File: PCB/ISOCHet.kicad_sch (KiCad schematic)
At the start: 19 parts, among them J1 USB_C_Receptacle_USB2.0, J2 Conn_01x08_Pin, SW0 BOOT, SW1 TAB, SW2 ENTER, SW3 CAPS, SW4 CAPS_STEP1.5, SW5 CAPS_STEP1.25, U1 CH552G, U2 USBLC6-2P6

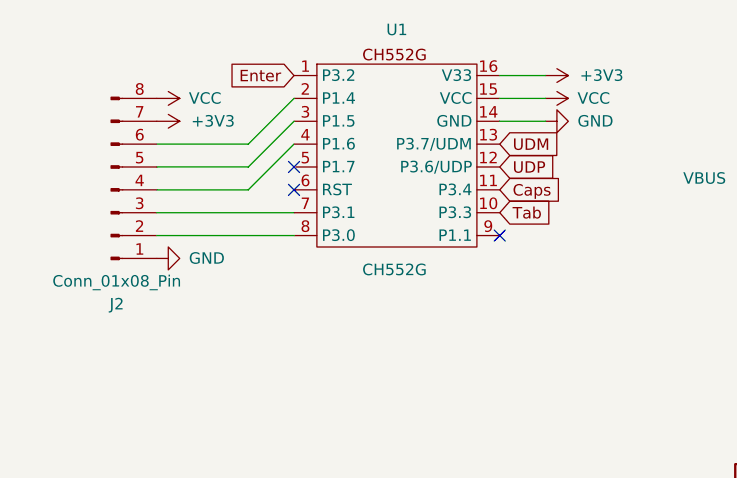
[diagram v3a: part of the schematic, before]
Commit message: Move components
 * Move decoupling capacitor C1 close to U1
 * Move U1 away from PCB edge
 * Align U1 with PCB centreline
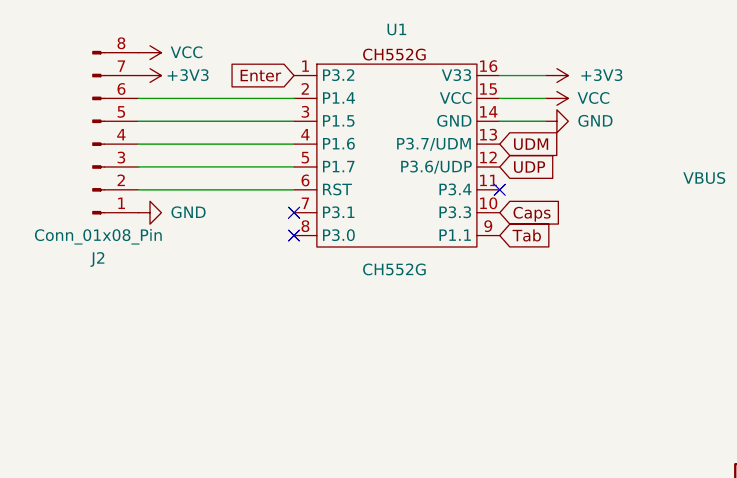
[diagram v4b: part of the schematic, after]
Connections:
- net Caps: now also U1.10 (P3.3); no longer U1.11 (P3.4)
- net Tab: now also U1.9 (P1.1); no longer U1.10 (P3.3)
- net at J2.2 (Pin_2): now also U1.6 (RST); no longer U1.8 (P3.0)
- net at J2.3 (Pin_3): now also U1.5 (P1.7); no longer U1.7 (P3.1)
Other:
- moved on the sheet: J2
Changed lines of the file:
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@@
   (junction (at 60.96 118.11) (diameter 0) (color 0 0 0 0)
   )
+  (no_connect (at 42.164 54.61))
   (no_connect (at 60.96 134.62))
-  (no_connect (at 42.164 46.99))
-  (no_connect (at 65.024 54.61))
+  (no_connect (at 65.024 49.53))
   (no_connect (at 60.96 132.08))
-  (no_connect (at 42.164 49.53))
+  (no_connect (at 42.164 52.07))
   (wire (pts (xy 120.65 48.26) (xy 115.57 48.26))
     (stroke (width 0) (type default))
@@
     (stroke (width 0) (type default))
   )
-  (wire (pts (xy 26.924 49.53) (xy 37.084 49.53))
-    (stroke (width 0) (type default))
-  )
   (wire (pts (xy 60.96 118.11) (xy 60.96 119.38))
     (stroke (width 0) (type default))
@@
     (stroke (width 0) (type default))
   )
-  (wire (pts (xy 26.924 46.99) (xy 37.084 46.99))
+  (wire (pts (xy 24.892 46.99) (xy 42.164 46.99))
     (stroke (width 0) (type default))
   )
@@
     (stroke (width 0) (type default))
   )
+  (wire (pts (xy 24.892 39.37) (xy 42.164 39.37))
+    (stroke (width 0) (type default))
+  )
   (wire (pts (xy 116.586 109.22) (xy 119.126 109.22))
     (stroke (width 0) (type default))
@@
     (stroke (width 0) (type default))
   )
-  (wire (pts (xy 26.924 52.07) (xy 42.164 52.07))
-    (stroke (width 0) (type default))
-  )
-  (wire (pts (xy 26.924 54.61) (xy 42.164 54.61))
-    (stroke (width 0) (type default))
-  )
   (wire (pts (xy 65.024 36.83) (xy 70.104 36.83))
     (stroke (width 0) (type default))
   )
-  (wire (pts (xy 37.084 46.99) (xy 42.164 41.91))
-    (stroke (width 0) (type default))
-  )
   (wire (pts (xy 115.57 53.34) (xy 115.57 48.26))
     (stroke (width 0) (type default))
@@
     (stroke (width 0) (type default))
   )
-  (wire (pts (xy 37.084 49.53) (xy 42.164 44.45))
-    (stroke (width 0) (type default))
-  )
   (wire (pts (xy 123.19 60.96) (xy 123.19 63.5))
     (stroke (width 0) (type default))
@@
     (stroke (width 0) (type default))
   )
+  (wire (pts (xy 24.892 41.91) (xy 42.164 41.91))
+    (stroke (width 0) (type default))
+  )
   (wire (pts (xy 71.374 111.76) (xy 60.96 111.76))
     (stroke (width 0) (type default))
@@
     (stroke (width 0) (type default))
   )
-  (wire (pts (xy 37.084 44.45) (xy 42.164 39.37))
-    (stroke (width 0) (type default))
-  )
-  (wire (pts (xy 26.924 44.45) (xy 37.084 44.45))
+  (wire (pts (xy 24.892 44.45) (xy 42.164 44.45))
     (stroke (width 0) (type default))
   )
   (wire (pts (xy 78.994 109.22) (xy 78.994 110.49))
+    (stroke (width 0) (type default))
+  )
+  (wire (pts (xy 24.892 49.53) (xy 42.164 49.53))
     (stroke (width 0) (type default))
   )
@@
     )
   )
-  (global_label "Tab" (shape input) (at 65.024 52.07 0) (fields_autoplaced)
+  (global_label "Tab" (shape input) (at 65.024 54.61 0) (fields_autoplaced)
     (effects (font (size 1.27 1.27)) (justify left))
-    (property "Intersheetrefs" "${INTERSHEET_REFS}" (at 71.2748 52.07 0)
+    (property "Intersheetrefs" "${INTERSHEET_REFS}" (at 71.2748 54.61 0)
       (effects (font (size 1.27 1.27)) (justify left) hide)
     )
@@
     )
   )
-  (global_label "Caps" (shape input) (at 65.024 49.53 0) (fields_autoplaced)
+  (global_label "Caps" (shape input) (at 65.024 52.07 0) (fields_autoplaced)
     (effects (font (size 1.27 1.27)) (justify left))
-    (property "Intersheetrefs" "${INTERSHEET_REFS}" (at 72.6053 49.53 0)
+    (property "Intersheetrefs" "${INTERSHEET_REFS}" (at 72.6053 52.07 0)
       (effects (font (size 1.27 1.27)) (justify left) hide)
     )
@@
     )
   )
-  (symbol (lib_id "power:+3V3") (at 26.924 41.91 270) (unit 1)
+  (symbol (lib_id "power:+3V3") (at 24.892 36.83 270) (unit 1)
     (in_bom yes) (on_board yes) (dnp no)
-    (property "Reference" "#PWR020" (at 23.114 41.91 0)
-      (effects (font (size 1.27 1.27)) hide)
-    )
-    (property "Value" "+3V3" (at 30.734 41.91 90)
-      (effects (font (size 1.27 1.27)) (justify left))
-    )
-    (property "Footprint" "" (at 26.924 41.91 0)
-      (effects (font (size 1.27 1.27)) hide)
-    )
-    (property "Datasheet" "" (at 26.924 41.91 0)
+    (property "Reference" "#PWR020" (at 21.082 36.83 0)
+      (effects (font (size 1.27 1.27)) hide)
+    )
+    (property "Value" "+3V3" (at 27.94 36.83 90)
+      (effects (font (size 1.27 1.27)) (justify left))
+    )
+    (property "Footprint" "" (at 24.892 36.83 0)
+      (effects (font (size 1.27 1.27)) hide)
+    )
+    (property "Datasheet" "" (at 24.892 36.83 0)
       (effects (font (size 1.27 1.27)) hide)
     )
@@
     )
   )
-  (symbol (lib_id "power:VCC") (at 26.924 39.37 270) (unit 1)
-    (in_bom yes) (on_board yes) (dnp no) (fields_autoplaced)
-    (property "Reference" "#PWR022" (at 23.114 39.37 0)
-      (effects (font (size 1.27 1.27)) hide)
-    )
-    (property "Value" "VCC" (at 30.48 39.37 90)
-      (effects (font (size 1.27 1.27)) (justify left))
-    )
-    (property "Footprint" "" (at 26.924 39.37 0)
-      (effects (font (size 1.27 1.27)) hide)
-    )
-    (property "Datasheet" "" (at 26.924 39.37 0)
+  (symbol (lib_id "power:VCC") (at 24.892 34.29 270) (unit 1)
+    (in_bom yes) (on_board yes) (dnp no)
+    (property "Reference" "#PWR022" (at 21.082 34.29 0)
+      (effects (font (size 1.27 1.27)) hide)
+    )
+    (property "Value" "VCC" (at 28.448 34.29 90)
+      (effects (font (size 1.27 1.27)) (justify left))
+    )
+    (property "Footprint" "" (at 24.892 34.29 0)
+      (effects (font (size 1.27 1.27)) hide)
+    )
+    (property "Datasheet" "" (at 24.892 34.29 0)
       (effects (font (size 1.27 1.27)) hide)
     )
@@
     )
   )
-  (symbol (lib_id "power:GND") (at 26.924 57.15 90) (unit 1)
-    (in_bom yes) (on_board yes) (dnp no) (fields_autoplaced)
-    (property "Reference" "#PWR021" (at 33.274 57.15 0)
-      (effects (font (size 1.27 1.27)) hide)
-    )
-    (property "Value" "GND" (at 30.48 57.15 90)
+  (symbol (lib_id "power:GND") (at 24.892 52.07 90) (unit 1)
+    (in_bom yes) (on_board yes) (dnp no) (fields_autoplaced)
+    (property "Reference" "#PWR021" (at 31.242 52.07 0)
+      (effects (font (size 1.27 1.27)) hide)
+    )
+    (property "Value" "GND" (at 28.448 52.07 90)
       (effects (font (size 1.27 1.27)) (justify right))
     )
-    (property "Footprint" "" (at 26.924 57.15 0)
-      (effects (font (size 1.27 1.27)) hide)
-    )
-    (property "Datasheet" "" (at 26.924 57.15 0)
+    (property "Footprint" "" (at 24.892 52.07 0)
+      (effects (font (size 1.27 1.27)) hide)
+    )
+    (property "Datasheet" "" (at 24.892 52.07 0)
       (effects (font (size 1.27 1.27)) hide)
     )
@@
     )
   )
-  (symbol (lib_id "Connector:Conn_01x08_Pin") (at 21.844 49.53 0) (mirror x) (unit 1)
+  (symbol (lib_id "Connector:Conn_01x08_Pin") (at 19.812 44.45 0) (mirror x) (unit 1)
     (in_bom no) (on_board yes) (dnp no)
-    (property "Reference" "J2" (at 22.479 62.23 0)
-      (effects (font (size 1.27 1.27)))
-    )
-    (property "Value" "Conn_01x08_Pin" (at 22.479 59.69 0)
-      (effects (font (size 1.27 1.27)))
-    )
-    (property "Footprint" "Connector_PinHeader_1.27mm:PinHeader_1x08_P1.27mm_Vertical" (at 21.844 49.53 0)
-      (effects (font (size 1.27 1.27)) hide)
-    )
-    (property "Datasheet" "~" (at 21.844 49.53 0)
-      (effects (font (size 1.27 1.27)) hide)
-    )
+    (property "Reference" "J2" (at 20.447 57.15 0)
+      (effects (font (size 1.27 1.27)))
+    )
+    (property "Value" "Conn_01x08_Pin" (at 20.447 54.61 0)
+      (effects (font (size 1.27 1.27)))
+    )
+    (property "Footprint" "Connector_PinHeader_1.27mm:PinHeader_1x08_P1.27mm_Vertical" (at 19.812 44.45 0)
+      (effects (font (size 1.27 1.27)) hide)
+    )
+    (property "Datasheet" "~" (at 19.812 44.45 0)
+      (effects (font (size 1.27 1.27)) hide)
+    )

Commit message: Use larger footprint for J2 header
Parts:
- J2: footprint Connector_PinHeader_1.27mm:PinHeader_1x08_P1.27mm_Vertical -> Connector_PinHeader_2.54mm:PinHeader_1x08_P2.54mm_Vertical
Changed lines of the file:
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@@
       (effects (font (size 1.27 1.27)))
     )
-    (property "Footprint" "Connector_PinHeader_1.27mm:PinHeader_1x08_P1.27mm_Vertical" (at 19.812 44.45 0)
+    (property "Footprint" "Connector_PinHeader_2.54mm:PinHeader_1x08_P2.54mm_Vertical" (at 19.812 44.45 0)
       (effects (font (size 1.27 1.27)) hide)
     )

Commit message: Use Alps SKQG switch for BOOT, update LCSC part numbers, add DigiKey part numbers
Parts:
- C1, C2: DigiKey (none) -> 1276-1005; LCSC (none) -> C66501; LSCC C1525 -> (none)
- D1: DigiKey (none) -> 1727-4326; LCSC (none) -> C2837790; LSCC C2837790 -> (none)
- F1: DigiKey (none) -> MF-FSMF050X; LCSC (none) -> C210357; LSCC C210357 -> (none)
- J1: DigiKey (none) -> 664-GSB1C211110DS1HR; LCSC (none) -> C2840393
- J2: footprint Connector_PinHeader_2.54mm:PinHeader_1x08_P2.54mm_Vertical -> Connector_PinHeader_2.00mm:PinHeader_1x08_P2.00mm_Vertical
- R1, R2: DigiKey (none) -> 311-5.10KHR; LCSC (none) -> C23186; LSCC C25905 -> (none)
- R3: DigiKey (none) -> 311-10.0KHR; LCSC (none) -> C25804; LSCC C25744 -> (none)
- SW0: footprint Button_Switch_SMD:SW_SPST_CK_KXT3 -> Button_Switch_SMD:SW_SPST_SKQG_WithStem; DigiKey (none) -> 4809-SKQGABE010; LCSC (none) -> C115351; LSCC C221821 -> (none)
- U1: DigiKey (none) -> n/a; LCSC (none) -> C111292; LSCC C111292 -> (none)
- U2: DigiKey (none) -> 497-5235; LCSC (none) -> C2687116; LSCC C2687116 -> (none)
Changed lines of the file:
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@@
       (effects (font (size 1.27 1.27)) hide)
     )
-    (property "LSCC" "C25744" (at 122.936 109.22 90)
+    (property "LCSC" "C25804" (at 122.936 109.22 90)
+      (effects (font (size 1.27 1.27)) hide)
+    )
+    (property "DigiKey" "311-10.0KHR" (at 122.936 109.22 90)
       (effects (font (size 1.27 1.27)) hide)
     )
@@
       (effects (font (size 1.27 1.27)) hide)
     )
-    (property "Datasheet" "https://www.usb.org/sites/default/files/documents/usb_type-c.zip" (at 49.53 119.38 0)
+    (property "Datasheet" "" (at 49.53 119.38 0)
+      (effects (font (size 1.27 1.27)) hide)
+    )
+    (property "LCSC" "C2840393" (at 45.72 119.38 0)
+      (effects (font (size 1.27 1.27)) hide)
+    )
+    (property "DigiKey" "664-GSB1C211110DS1HR" (at 45.72 119.38 0)
       (effects (font (size 1.27 1.27)) hide)
     )
@@
       (effects (font (size 1.27 1.27)) hide)
     )
-    (property "LSCC" "C2687116" (at 98.806 87.63 0)
+    (property "LCSC" "C2687116" (at 98.806 87.63 0)
+      (effects (font (size 1.27 1.27)) hide)
+    )
+    (property "DigiKey" "497-5235" (at 98.806 87.63 0)
       (effects (font (size 1.27 1.27)) hide)
     )
@@
       (effects (font (size 1.27 1.27)) hide)
     )
-    (property "LSCC" "C25905" (at 75.184 109.22 90)
+    (property "LCSC" "C23186" (at 75.184 109.22 90)
+      (effects (font (size 1.27 1.27)) hide)
+    )
+    (property "DigiKey" "311-5.10KHR" (at 75.184 109.22 90)
       (effects (font (size 1.27 1.27)) hide)
     )
@@
       (effects (font (size 1.27 1.27)) hide)
     )
-    (property "LSCC" "C2837790" (at 109.22 48.26 0)
+    (property "LCSC" "C2837790" (at 109.22 48.26 0)
+      (effects (font (size 1.27 1.27)) hide)
+    )
+    (property "DigiKey" "1727-4326" (at 109.22 48.26 0)
       (effects (font (size 1.27 1.27)) hide)
     )
@@
       (effects (font (size 1.27 1.27)) hide)
     )
-    (property "LSCC" "C210357" (at 99.06 48.26 90)
+    (property "LCSC" "C210357" (at 99.06 48.26 90)
+      (effects (font (size 1.27 1.27)) hide)
+    )
+    (property "DigiKey" "MF-FSMF050X" (at 99.06 48.26 90)
       (effects (font (size 1.27 1.27)) hide)
     )
@@
       (effects (font (size 1.27 1.27)))
     )
-    (property "Footprint" "Button_Switch_SMD:SW_SPST_CK_KXT3" (at 134.366 104.14 0)
+    (property "Footprint" "Button_Switch_SMD:SW_SPST_SKQG_WithStem" (at 134.366 104.14 0)
       (effects (font (size 1.27 1.27)) hide)
     )
@@
       (effects (font (size 1.27 1.27)) hide)
     )
-    (property "LSCC" "C221821" (at 134.366 109.22 0)
+    (property "LCSC" "C115351" (at 134.366 109.22 0)
+      (effects (font (size 1.27 1.27)) hide)
+    )
+    (property "DigiKey" "4809-SKQGABE010" (at 134.366 109.22 0)
       (effects (font (size 1.27 1.27)) hide)
     )
@@
       (effects (font (size 1.27 1.27)) hide)
     )
-    (property "LSCC" "C1525" (at 115.57 57.15 0)
+    (property "LCSC" "C66501" (at 115.57 57.15 0)
+      (effects (font (size 1.27 1.27)) hide)
+    )
+    (property "DigiKey" "1276-1005" (at 115.57 57.15 0)
       (effects (font (size 1.27 1.27)) hide)
     )
@@
       (effects (font (size 1.27 1.27)))
     )
-    (property "Footprint" "Connector_PinHeader_2.54mm:PinHeader_1x08_P2.54mm_Vertical" (at 19.812 44.45 0)
+    (property "Footprint" "Connector_PinHeader_2.00mm:PinHeader_1x08_P2.00mm_Vertical" (at 19.812 44.45 0)
       (effects (font (size 1.27 1.27)) hide)
     )
@@
       (effects (font (size 1.27 1.27)) hide)
     )
-    (property "LSCC" "C1525" (at 130.81 57.15 0)
+    (property "LCSC" "C66501" (at 130.81 57.15 0)
+      (effects (font (size 1.27 1.27)) hide)
+    )
+    (property "DigiKey" "1276-1005" (at 130.81 57.15 0)
       (effects (font (size 1.27 1.27)) hide)
     )
@@
       (effects (font (size 1.27 1.27)) hide)
     )
-    (property "LSCC" "C25905" (at 75.184 111.76 90)
+    (property "LCSC" "C23186" (at 75.184 111.76 90)
+      (effects (font (size 1.27 1.27)) hide)
+    )
+    (property "DigiKey" "311-5.10KHR" (at 75.184 111.76 90)
       (effects (font (size 1.27 1.27)) hide)
     )
@@
       (effects (font (size 1.27 1.27)) hide)
     )
-    (property "LSCC" "C111292" (at 53.34 45.72 0)
-      (effects (font (size 1.27 1.27)) hide)
-    )
+    (property "LCSC" "C111292" (at 53.34 45.72 0)
+      (effects (font (size 1.27 1.27)) hide)
+    )
+    (property "DigiKey" "n/a" (at 53.34 45.72 0)
+      (effects (font (size 1.27 1.27)) hide)
+    )

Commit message: Change footprint for USB port
USB C socket is now GSB1C211110DS1HR instead of GCT USB4085. Update routing with more filleting on 90° corners.
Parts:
- J1: footprint Connector_USB:USB_C_Receptacle_GCT_USB4085 -> Project Library:GSB1C211110DS1HR
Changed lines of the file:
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@@
       (effects (font (size 1.27 1.27)))
     )
-    (property "Footprint" "Connector_USB:USB_C_Receptacle_GCT_USB4085" (at 49.53 119.38 0)
+    (property "Footprint" "Project Library:GSB1C211110DS1HR" (at 49.53 119.38 0)
       (effects (font (size 1.27 1.27)) hide)
     )
